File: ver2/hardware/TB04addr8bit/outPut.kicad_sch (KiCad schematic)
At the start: 0 parts

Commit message: ver2: 命令ラッチを1相ずらし、アドレスMUXを完成、I/Oと周辺ICを配置
- 命令ラッチの取り込みエッジを1相ずらし(U20 Cp=FCH1→FCH2 /
  U26 Cp=FCH2→DCR)。EXE中はアドレスバスがmAddrになるため、
  従来はEXE→FCH1の境目でROMのアクセスが間に合わなかった
- /OE_ROM のゲート入力を ~WE から ~WR へ付け替え
  (レジスタ書込許可ではなくメモリ書込で判定するのが正)
- PCの161出力をアドレスバスから切り離し、244経由に変更
  U42(PC)/U43(mAddr)/U44(SP)の入出力を結線し A0-A7 を駆動
  U44は 11110+SP[2:0] で 0xF0-0xF7 を生成。IN/OUT用の244は廃止
- PCのカウントイネーブルを 74LS32 の空きゲートで FCH1|FCH2 として生成
- PC_mAddr シートを PC へ改称し、分岐ロード用の 8bit 2:1 MUX
  (74LS157×2, U14/U15)を新設。出力 PC0-7 を161のD入力へ
  PCカウンタ(IC9/IC10)は addrMUX シートへ移動
- 6116 の /CS にゲートを追加(P2 & !P5)、D4-D7 にラベルを付与
- Yドライバ(74HC244×2, U16/U17)、inPort の 74LS253×2、
  outPort の 74HC273+LED4個 を配置(結線は未)
- ルートから未参照だった ROM_ALU_Decoder / interFace / RS02 を削除

未了: 共通8bitデータバス、オペランド源MUX(SEL_A/SEL_B/SEL_IMM/SEL_Y)、
I/Oポートの結線。PC_mAddr.kicad_sch は PC.kicad_sch と同一内容の
残骸として残っている

Co-Authored-By: Claude Opus 5 <noreply@anthropic.com>
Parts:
- added D66, D67, D68, D69: LED, LED_THT:LED_D3.0mm_Clear, symbol Device:LED
- added RN11: 4.7K, Resistor_THT:R_Array_SIP5, symbol Device:R_Network04
- added U47: 74HC273, symbol 74xx:74HC273
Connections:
- new net: D66.1 (K), RN11.5 (R4)
- new net: D69.1 (K), RN11.2 (R1)
- new net: D67.1 (K), RN11.4 (R3)
- new net: D68.1 (K), RN11.3 (R2)
- new net GND: RN11.1 (common)

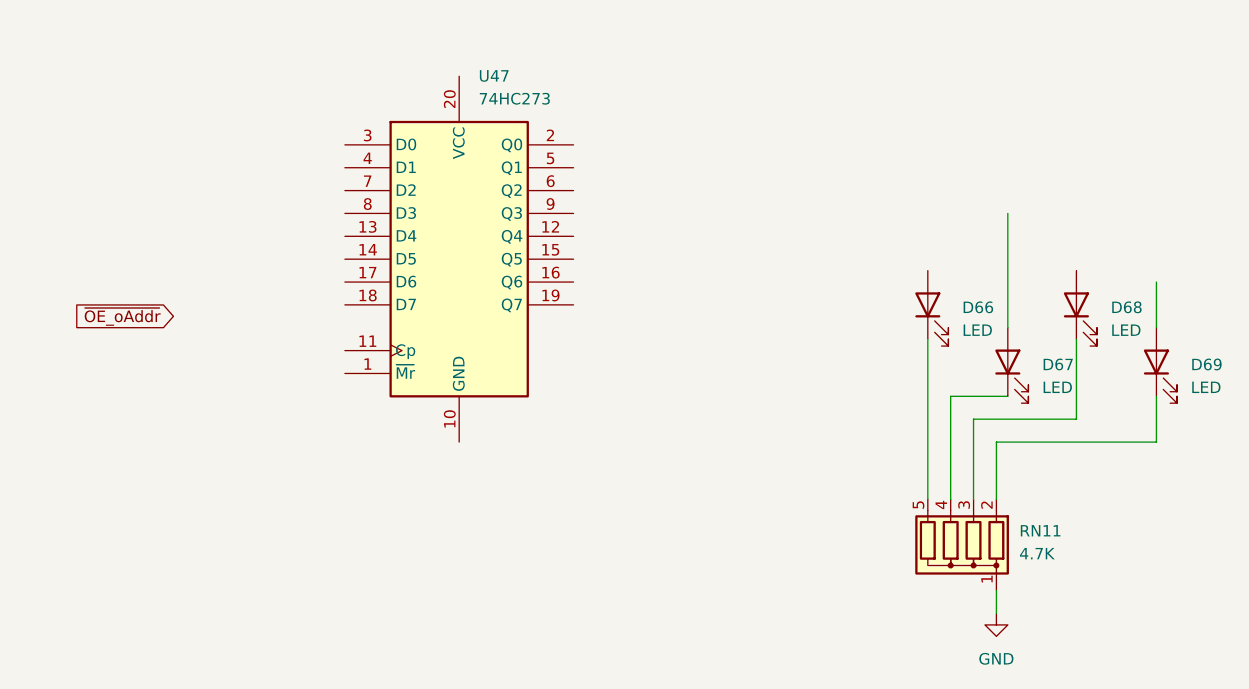
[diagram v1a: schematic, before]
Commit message: ver2: 要修正5件を修正し共通データバス・オペランド源MUX・I/Oを結線
- 6116の/CS極性を修正し、スタック域を含むRAM_STK_SEL(0xC0-0xF7)に統一
- ALU出力をDI0-3へ直結、U21はYドライバ源として残す(LD/POP/RET対策)
- 共通8bitデータバスMD0-7を新設(ROM/RAM/Yドライバ/IN244が排他駆動)
- aポートMUX(74LS253x2)・IN用244・Yドライバ制御ゲートを追加
- IN実行時のROM競合を/OE_ROMに~OE_iAddrを足して回避
- 4bit書込時にMD4-7が浮くのをU17 bank2で0駆動
- 74LS157のEをGND固定、孤立したPC_mAddrシートを削除

Co-Authored-By: Claude Opus 5 <noreply@anthropic.com>
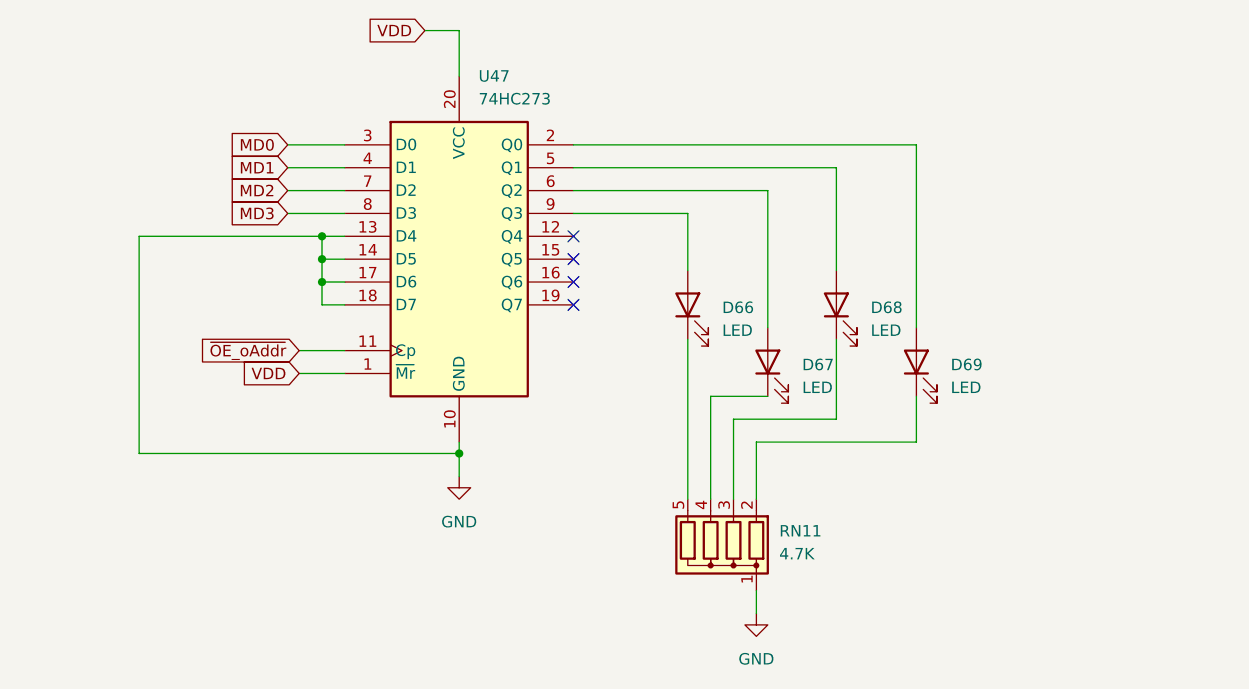
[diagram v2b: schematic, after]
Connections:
- net GND: now also U47.10 (GND), U47.13 (D4), U47.14 (D5), U47.17 (D6), U47.18 (D7)
- net ~{OE_oAddr}: now also U47.11 (Cp)
- net at D66.2 (A): now also U47.9 (Q3)
- net VDD: now reaches U47.1 (~{Mr})
- net VDD: now also U47.20 (VCC)
- net at U47.2 (Q0): now also D69.2 (A)
- net MD0: now reaches U47.3 (D0)
- net MD1: now reaches U47.4 (D1)
- net at U47.5 (Q1): now also D68.2 (A)
- net at U47.6 (Q2): now also D67.2 (A)
- net MD2: now reaches U47.7 (D2)
- net MD3: now reaches U47.8 (D3)
- no-connect marks 0 -> 4
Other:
- moved on the sheet: D66, D67, D68, D69, RN11

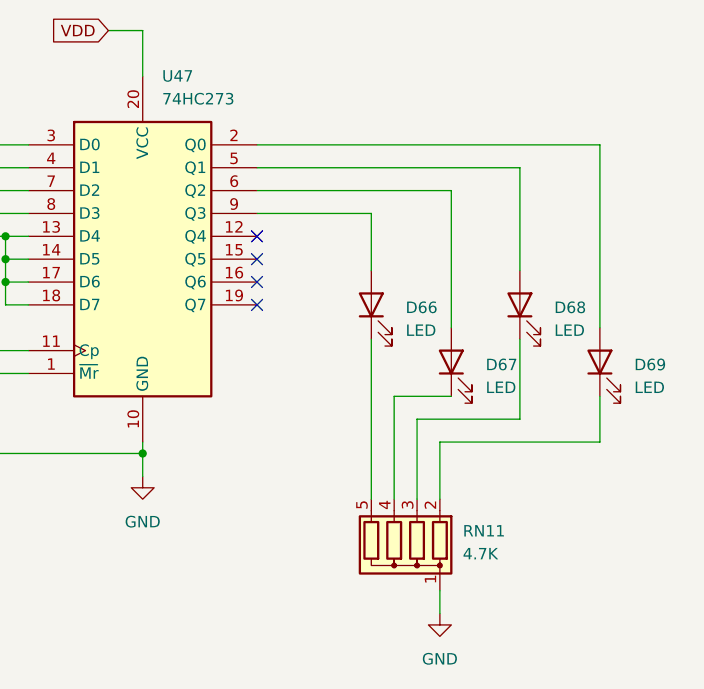
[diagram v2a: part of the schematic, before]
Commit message: ver2: ゲートICをgatesシートへ集約しアノテーションを掛け直し
- 分散していた8パッケージ(U1/U2/U5/U25/U35/U36/U37/U51)をgatesシートへ集約
- シートをまたぐ11本をグローバルラベル化(~P4/~P5/~OUT_SEL/~CS_RAM/
  ~OE_ROM/CLK_C/CLK_Z/PC_CNT_EN/~PC_PE/~Ena_RS01/~Enb_RS01)
- U40のP2入力がROM_SELに吸着していたのを修正(RAM_SELが逆条件だった)
- !P5の重複インバータを解消、未使用ゲート入力7本をGNDへ
- ALU入力MUXをinPut→PC、PCカウンタをaddrMUX→PCへ移動
- 全体を再アノテーション(シート順採番)。旧→新の対応は電気的変化なしを確認

Co-Authored-By: Claude Opus 5 <noreply@anthropic.com>
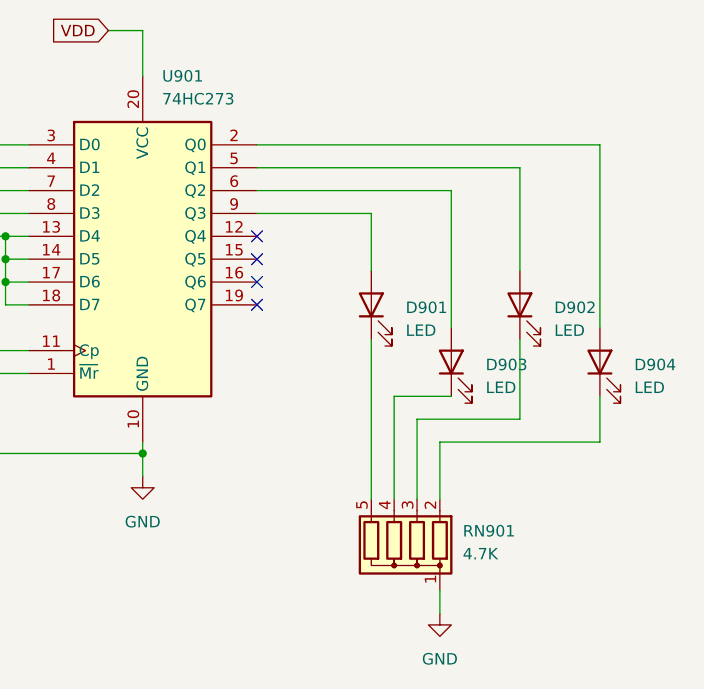
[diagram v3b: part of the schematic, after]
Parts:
- renumbered D66 to D901, D68 to D902, D67 to D903, D69 to D904, RN11 to RN901, U47 to U901
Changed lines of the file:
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@@
 		(dnp no)
 		(fields_autoplaced yes)
-		(property "Reference" "D66"
+		(property "Reference" "D901"
 			(at 162.56 81.5974 90)
 			(show_name no)
@@
 			(project "TB04addr8bit"
 				(path "/d176c79b-dced-4d01-bcec-7dfd676fcfc2/0fcb6af9-236e-4ccd-af48-2dd0360a8279"
-					(reference "D66")
+					(reference "D901")
 					(unit 1)
 				)
@@
 		(dnp no)
 		(fields_autoplaced yes)
-		(property "Reference" "U47"
+		(property "Reference" "U901"
 			(at 135.4933 55.88 0)
 			(show_name no)
@@
 			(project "TB04addr8bit"
 				(path "/d176c79b-dced-4d01-bcec-7dfd676fcfc2/0fcb6af9-236e-4ccd-af48-2dd0360a8279"
-					(reference "U47")
+					(reference "U901")
 					(unit 1)
 				)
@@
 		(dnp no)
 		(fields_autoplaced yes)
-		(property "Reference" "D69"
+		(property "Reference" "D904"
 			(at 187.96 87.9474 90)
 			(show_name no)
@@
 			(project "TB04addr8bit"
 				(path "/d176c79b-dced-4d01-bcec-7dfd676fcfc2/0fcb6af9-236e-4ccd-af48-2dd0360a8279"
-					(reference "D69")
+					(reference "D904")
 					(unit 1)
 				)
@@
 		(dnp no)
 		(fields_autoplaced yes)
-		(property "Reference" "D67"
+		(property "Reference" "D903"
 			(at 171.45 87.9474 90)
 			(show_name no)
@@
 			(project "TB04addr8bit"
 				(path "/d176c79b-dced-4d01-bcec-7dfd676fcfc2/0fcb6af9-236e-4ccd-af48-2dd0360a8279"
-					(reference "D67")
+					(reference "D903")
 					(unit 1)
 				)
@@
 		(dnp no)
 		(fields_autoplaced yes)
-		(property "Reference" "D68"
+		(property "Reference" "D902"
 			(at 179.07 81.5974 90)
 			(show_name no)
@@
 			(project "TB04addr8bit"
 				(path "/d176c79b-dced-4d01-bcec-7dfd676fcfc2/0fcb6af9-236e-4ccd-af48-2dd0360a8279"
-					(reference "D68")
+					(reference "D902")
 					(unit 1)
 				)
@@
 		(dnp no)
 		(fields_autoplaced yes)
-		(property "Reference" "#PWR0154"
+		(property "Reference" "#PWR0901"
 			(at 133.35 106.68 0)
 			(hide yes)
@@
 			(project "TB04addr8bit"
 				(path "/d176c79b-dced-4d01-bcec-7dfd676fcfc2/0fcb6af9-236e-4ccd-af48-2dd0360a8279"
-					(reference "#PWR0154")
+					(reference "#PWR0901")
 					(unit 1)
 				)
@@
 		(dnp no)
 		(fields_autoplaced yes)
-		(property "Reference" "#PWR0144"
+		(property "Reference" "#PWR0902"
 			(at 166.37 121.92 0)
 			(hide yes)
@@
 			(project "TB04addr8bit"
 				(path "/d176c79b-dced-4d01-bcec-7dfd676fcfc2/0fcb6af9-236e-4ccd-af48-2dd0360a8279"
-					(reference "#PWR0144")
+					(reference "#PWR0902")
 					(unit 1)
 				)
@@
 		(in_pos_files yes)
 		(dnp no)
-		(property "Reference" "RN11"
+		(property "Reference" "RN901"
 			(at 168.91 106.4259 0)
 			(show_name no)
@@
 			(project "TB04addr8bit"
 				(path "/d176c79b-dced-4d01-bcec-7dfd676fcfc2/0fcb6af9-236e-4ccd-af48-2dd0360a8279"
-					(reference "RN11")
+					(reference "RN901")
 					(unit 1)
 				)

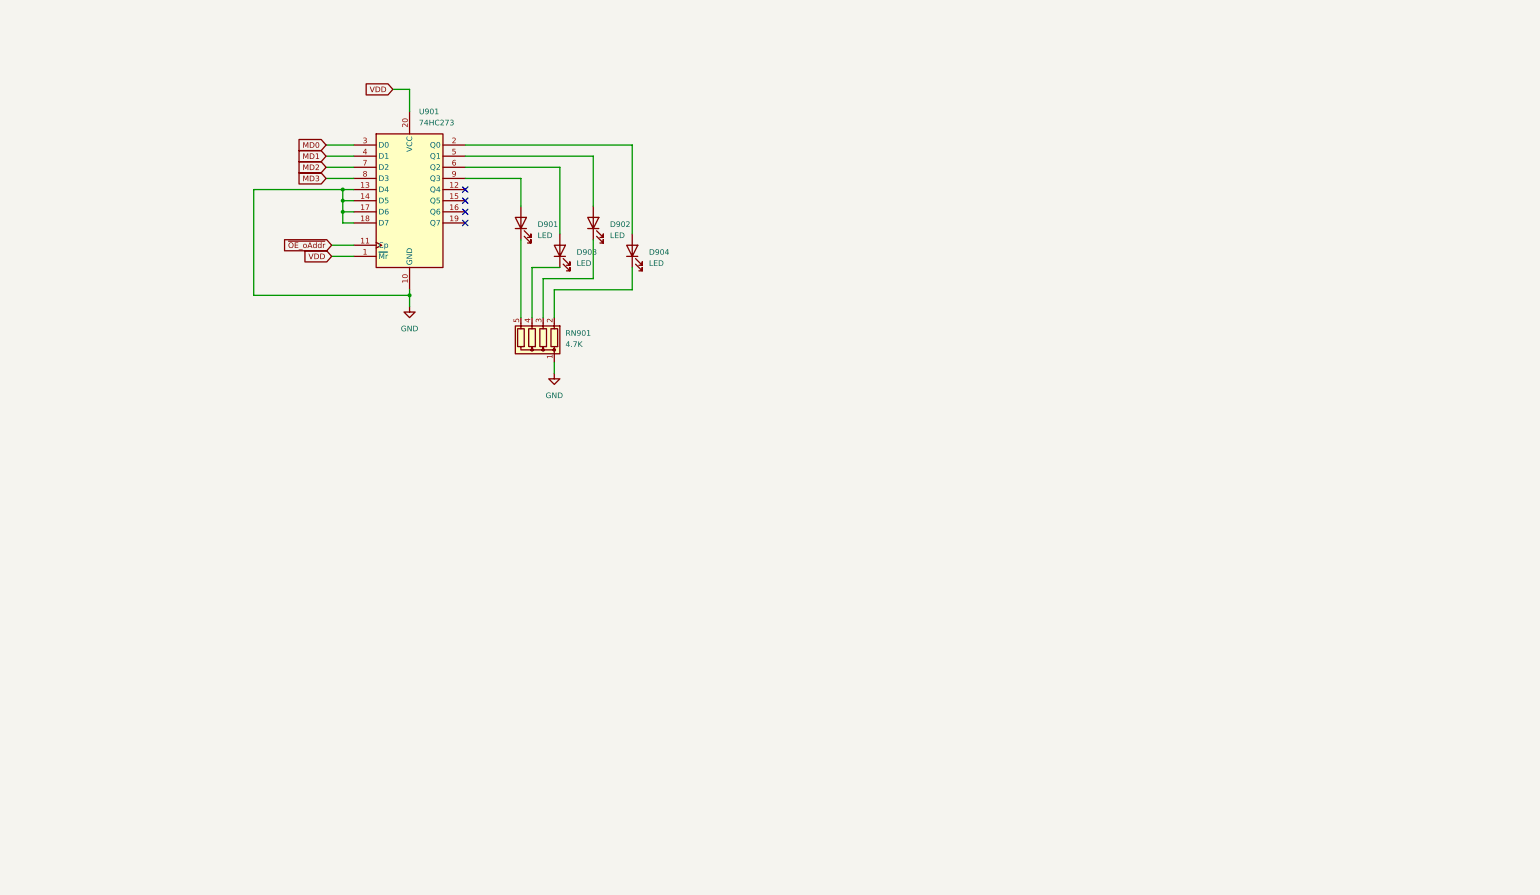
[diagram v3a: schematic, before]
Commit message: ver2: I/Oを4ch化しアドレスバスの浮きを解消(OUTは377化・RAMのCSをEXEゲート)
- I/Oアドレス源244・port位置MUX157・portデコード139を追加し、IN244×4/OUT×4に拡張。
  IN/OUT実行中も 0xF8|port / 0xFC|port をアドレスバスへ出すことで、全相・全命令で
  アドレスバスが必ず1つに駆動される状態にした(OUTのRAM誤書込・INのMD衝突を構造的に解消)。
- OUTポートを74HC273→74HC377へ。~E=139出力・CP=~CLK_CPUとし、クロックゲートなしで
  EXE中間の1回だけ取り込む(取り込み余裕が15ns→半相)。
- ~CS_RAM を !(RAM_STK_SEL & EXE) に変更(CS_RAMノード新設)。EXE末に出る第2の書込パルスを
  約38nsに短縮しtWP未満に収めた。フェッチ3相でRAMが非選択になる副次効果あり。
- OUTコネクタのピン配列を7segIF J1に合わせて入れ替え(D3出力がVDDへ短絡する組合せを回避)。
- パスコンが無かった2シート(outPort・PC_aluMux)に追加。RS.kicad_sch を RS00.kicad_sch へ改名。

Co-Authored-By: Claude Opus 5 <noreply@anthropic.com>
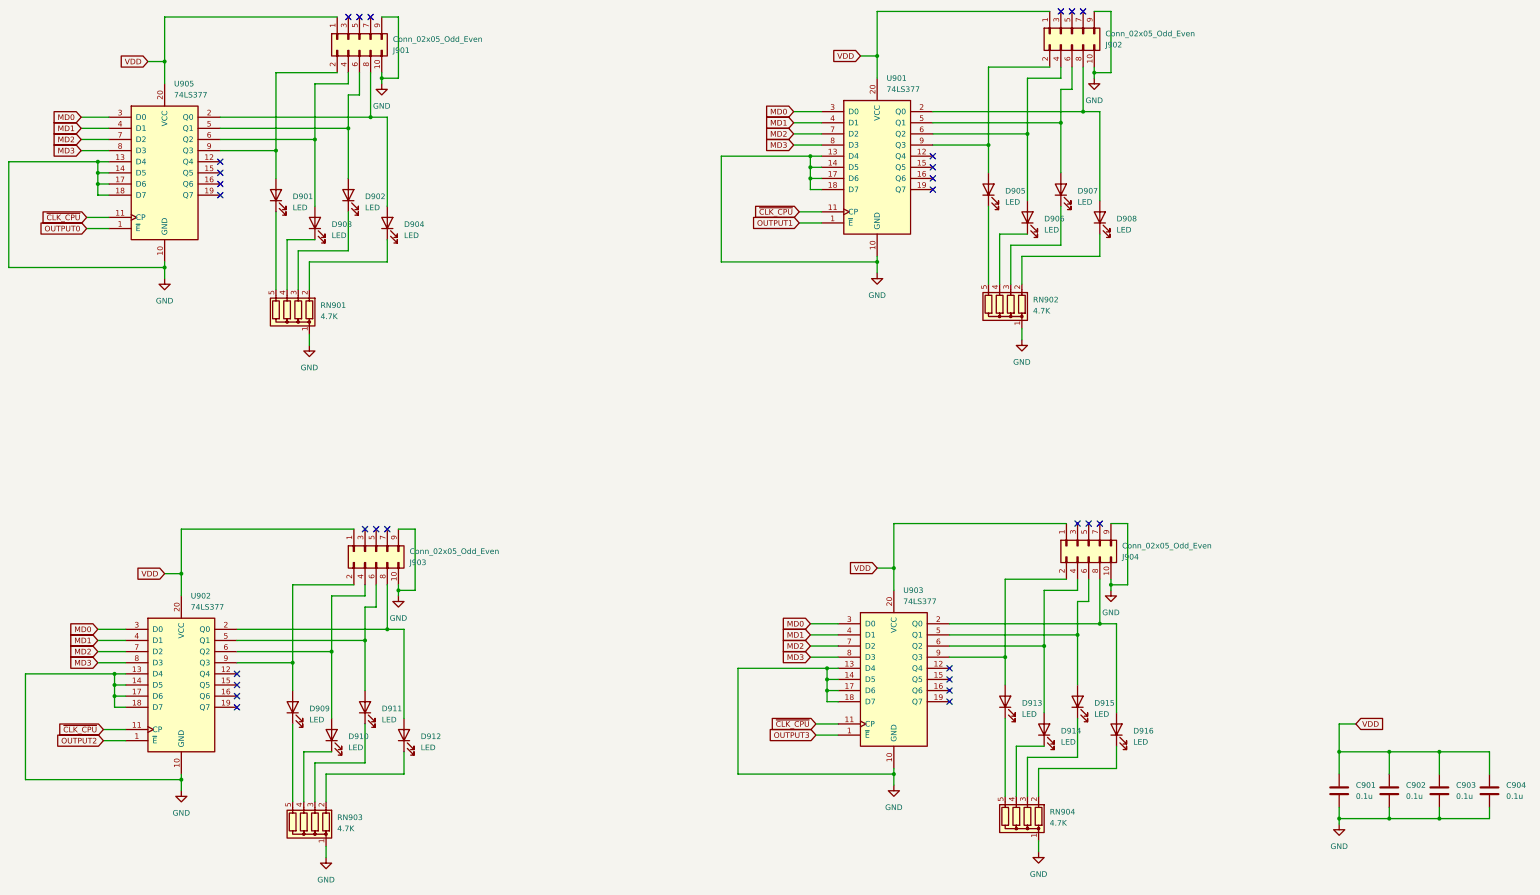
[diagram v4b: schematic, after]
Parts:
- removed U901: 74HC273, symbol 74xx:74HC273
- added C901, C902, C903, C904: 0.1u, symbol Device:C
- added D905, D906, D907, D908, D909, D910, D911, D912, D913, D914, D915, D916: LED, LED_THT:LED_D3.0mm_Clear, symbol Device:LED
- added J901, J902, J903, J904: Conn_02x05_Odd_Even, symbol Connector_Generic:Conn_02x05_Odd_Even
- added RN902, RN903, RN904: 4.7K, Resistor_THT:R_Array_SIP5, symbol Device:R_Network04
- added U901, U902, U903, U905: 74LS377, symbol 74xx:74LS377
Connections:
- net GND: now also C901.1, C902.1, C903.1, C904.1, J901.10 (Pin_10), J901.9 (Pin_9), J902.10 (Pin_10), J902.9 (Pin_9), J903.10 (Pin_10), J903.9 (Pin_9), J904.10 (Pin_10), J904.9 (Pin_9), RN902.1 (common), RN903.1 (common), RN904.1 (common), U901.10 (GND), U901.13 (D4), U901.14 (D5), U901.17 (D6), U901.18 (D7), U902.10 (GND), U902.13 (D4), U902.14 (D5), U902.17 (D6), U902.18 (D7), U903.10 (GND), U903.13 (D4), U903.14 (D5), U903.17 (D6), U903.18 (D7), U905.10 (GND), U905.13 (D4), U905.14 (D5), U905.17 (D6), U905.18 (D7)
- net MD0: now also U901.3 (D0), U902.3 (D0), U903.3 (D0), U905.3 (D0)
- net MD1: now also U901.4 (D1), U902.4 (D1), U903.4 (D1), U905.4 (D1)
- net MD2: now also U901.7 (D2), U902.7 (D2), U903.7 (D2), U905.7 (D2)
- net MD3: now also U901.8 (D3), U902.8 (D3), U903.8 (D3), U905.8 (D3)
- net VDD: now also C901.2, C902.2, C903.2, C904.2, J901.1 (Pin_1), J902.1 (Pin_1), J903.1 (Pin_1), J904.1 (Pin_1), U901.20 (VCC), U902.20 (VCC), U903.20 (VCC), U905.20 (VCC)
- net at D901.2 (A): now also J901.2 (Pin_2), U905.9 (Q3)
- net at D904.2 (A): now also J901.8 (Pin_8), U905.2 (Q0)
- net at D902.2 (A): now also J901.6 (Pin_6), U905.5 (Q1)
- net at D903.2 (A): now also J901.4 (Pin_4), U905.6 (Q2)
- new net: D905.1 (K), RN902.5 (R4)
- new net: D905.2 (A), J902.2 (Pin_2), U901.9 (Q3)
- new net: D913.2 (A), J904.2 (Pin_2), U903.9 (Q3)
- new net: D914.2 (A), J904.4 (Pin_4), U903.6 (Q2)
- new net: D915.2 (A), J904.6 (Pin_6), U903.5 (Q1)
- new net: D916.2 (A), J904.8 (Pin_8), U903.2 (Q0)
- new net: D909.2 (A), J903.2 (Pin_2), U902.9 (Q3)
- new net: D910.2 (A), J903.4 (Pin_4), U902.6 (Q2)
- new net: D911.2 (A), J903.6 (Pin_6), U902.5 (Q1)
- new net: D912.2 (A), J903.8 (Pin_8), U902.2 (Q0)
- new net: D914.1 (K), RN904.4 (R3)
- new net: D906.2 (A), J902.4 (Pin_4), U901.6 (Q2)
- new net: D907.2 (A), J902.6 (Pin_6), U901.5 (Q1)
- new net: D908.2 (A), J902.8 (Pin_8), U901.2 (Q0)
- new net: D907.1 (K), RN902.3 (R2)
- new net: D911.1 (K), RN903.3 (R2)
- new net: D906.1 (K), RN902.4 (R3)
- new net: D912.1 (K), RN903.2 (R1)
- new net: D916.1 (K), RN904.2 (R1)
- new net: D915.1 (K), RN904.3 (R2)
- new net: D909.1 (K), RN903.5 (R4)
- new net: D908.1 (K), RN902.2 (R1)
- new net: D913.1 (K), RN904.5 (R4)
- new net: D910.1 (K), RN903.4 (R3)
- new net OUTPUT0: U905.1 (~{E})
- new net OUTPUT1: U901.1 (~{E})
- new net OUTPUT2: U902.1 (~{E})
- new net OUTPUT3: U903.1 (~{E})
- new net ~{CLK_CPU}: U901.11 (CP), U902.11 (CP), U903.11 (CP), U905.11 (CP)
- no-connect marks 4 -> 28
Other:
- moved on the sheet: D901, D902, D903, D904, RN901
